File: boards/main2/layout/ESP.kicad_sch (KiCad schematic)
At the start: 15 parts, among them U13 ESP32-S3-MINI-1-N8

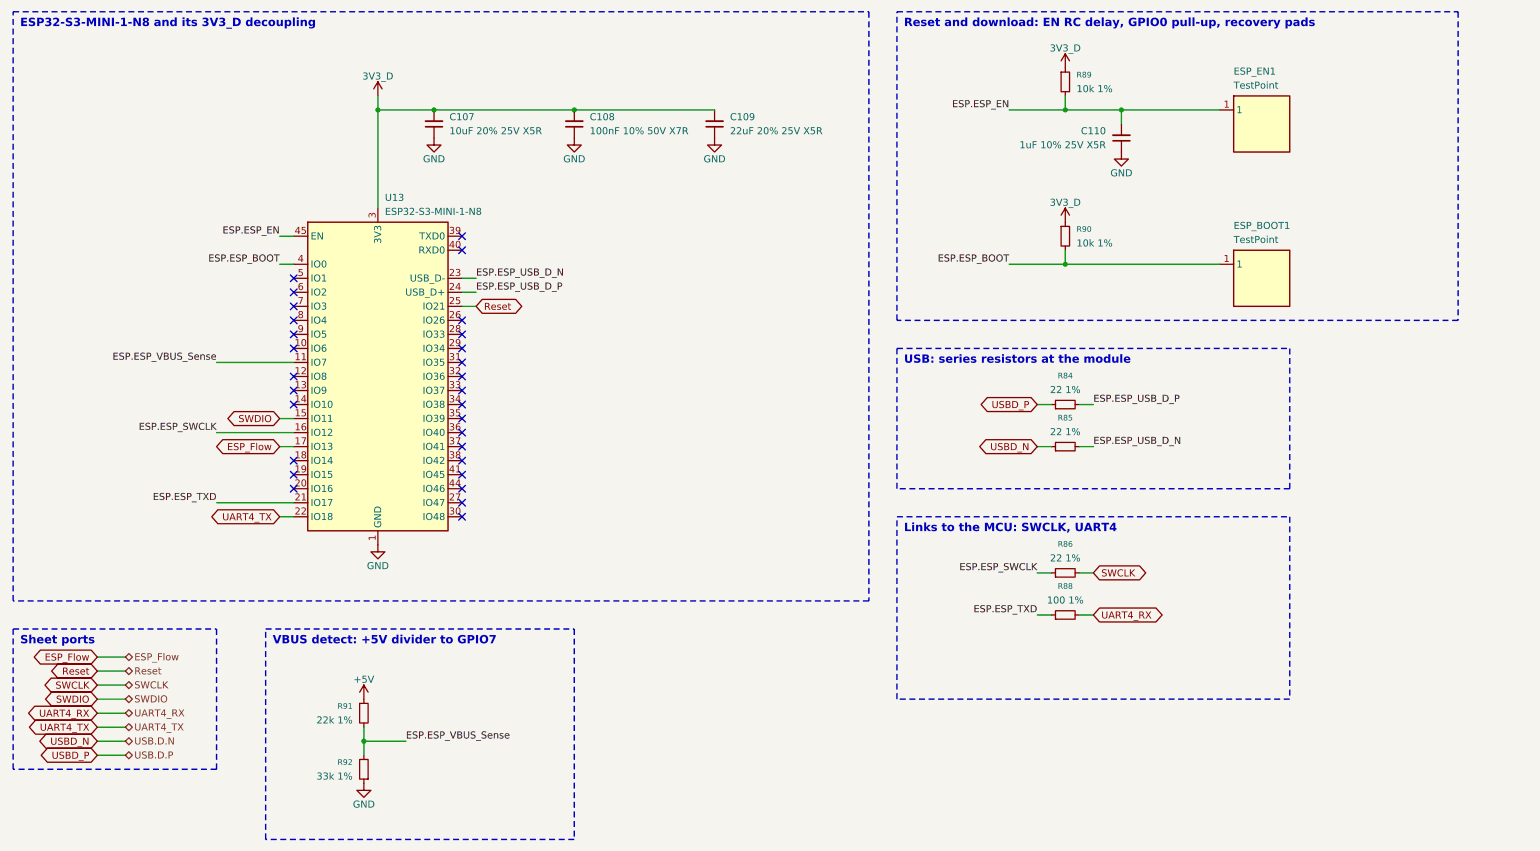
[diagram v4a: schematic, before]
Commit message: 🚧 Swap main2's USB and ESP32-S3 for an ESP32-C5 and programming headers
Schematic and component checkpoint; the layout follows in its own commit.

- Remove USB-C, its ESD, power path and VBUS sense; both MCUs flash over
  the air.
- U13 ESP32-C5-MINI-1-N4 (dual-band, 5 GHz channels 36-48) in the
  rear-right corner, with its antenna notch on the right edge. SW4 and its
  notch move to the rear-left.
- H7-C5 link: SPI2 half-duplex 3-wire (PA12 SCK, PA11 CSn, PB14 DATA with
  IOSWP), PA9 flow control, UART4 fallback on the same pins. Fan_Enable
  moves to PB10, IMU INT1 to PB6, INT2 is left open.
- J2: 2x3 1.27 mm header in the ESP-Prog layout. SWD1: 1x4 1.27 mm in
  clone ST-Link order (SWDIO, GND, SWCLK, 5V). 5V_IN feeds VSYS through
  D17 (B5819W) to flash without the battery.
- R44/R45 to 20k/2k keeps PC5 below its absolute maximum at the clamp.
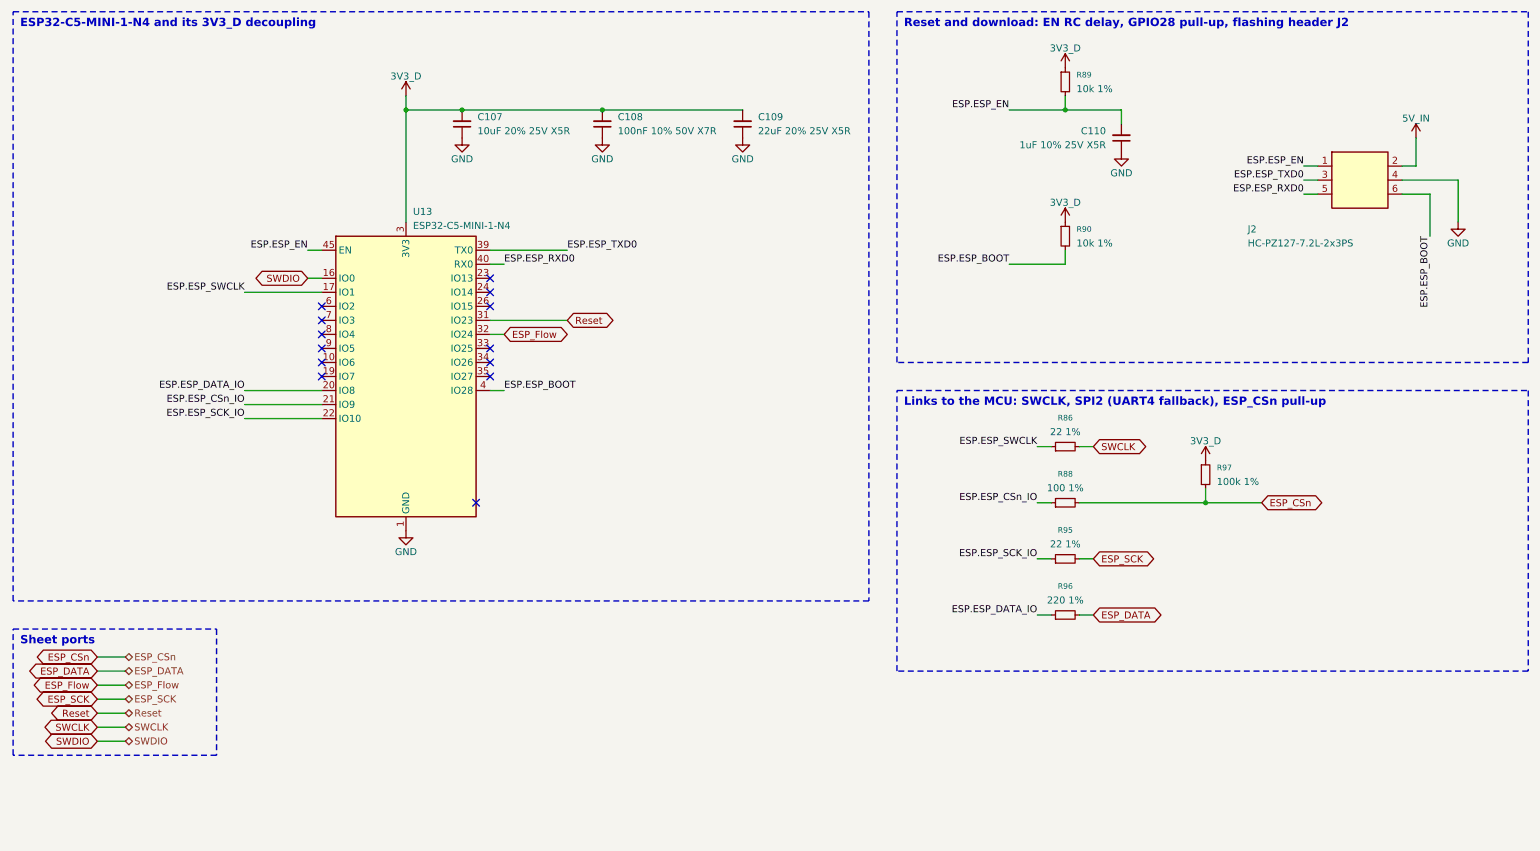
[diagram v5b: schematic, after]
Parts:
- removed ESP_BOOT1, ESP_EN1: TestPoint, Team-Micras_MicrasPCB_components_micras_TestPoint:TestPoint_Pad_D0.8mm, symbol TestPoint
- removed R84, R85: 22 1%, stdlib_kicad-footprints_Resistor_SMD:R_0402_1005Metric, symbol R_Small
- removed R91: 22k 1%, stdlib_kicad-footprints_Resistor_SMD:R_0402_1005Metric, symbol R_Small
- removed R92: 33k 1%, stdlib_kicad-footprints_Resistor_SMD:R_0402_1005Metric, symbol R_Small
- removed U13: ESP32-S3-MINI-1-N8, Team-Micras_MicrasPCB_components_espressif_ESP32-S3-MINI-1:ESP32-S3-MINI-1, symbol ESP32-S3-MINI-1
- added J2: HC-PZ127-7.2L-2x3PS, Team-Micras_MicrasPCB_components_hong-cheng_HC-PZ127-7.2L-2x3PS:HC-PZ127-7.2L-2x3PS, symbol HC-PZ127-7.2L-2x3PS
- added R95: 22 1%, stdlib_kicad-footprints_Resistor_SMD:R_0402_1005Metric, symbol R_Small
- added R96: 220 1%, stdlib_kicad-footprints_Resistor_SMD:R_0402_1005Metric, symbol R_Small
- added R97: 100k 1%, stdlib_kicad-footprints_Resistor_SMD:R_0402_1005Metric, symbol R_Small
- added U13: ESP32-C5-MINI-1-N4, Team-Micras_MicrasPCB_components_espressif_ESP32-C5-MINI-1:ESP32-C5-MINI-1, symbol ESP32-C5-MINI-1
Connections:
- net 3V3_D: now also R97.1, U13.3 (3V3)
- net ESP.ESP_BOOT: now also J2.6 (Pin_6), U13.4 (IO28)
- net ESP.ESP_EN: now also J2.1 (Pin_1), U13.45 (EN)
- net ESP.ESP_SWCLK: now also U13.17 (IO1)
- net ESP_Flow: now also U13.32 (IO24)
- net GND: now also J2.4 (Pin_4), U13.1 (GND), U13.2 (GND), U13.42 (GND), U13.43 (GND), U13.46 (GND), U13.47 (GND), U13.48 (GND), U13.50 (GND), U13.51 (GND), U13.52 (GND), U13.53 (GND), U13.54 (GND), U13.55 (GND), U13.56 (GND), U13.57 (GND), U13.58 (GND), U13.59 (GND), U13.60 (GND), U13.61 (GND), U13.62 (GND), U13.63 (GND), U13.64 (GND), U13.65 (GND)
- net Reset: now also U13.31 (IO23)
- net SWDIO: now also U13.16 (IO0)
- net ESP.ESP_TXD renamed ESP.ESP_CSn_IO
- net ESP.ESP_CSn_IO: now also U13.21 (IO9)
- net UART4_RX renamed ESP_CSn
- net ESP_CSn: now also R97.2
- new net: U13.11 (NC), U13.12 (NC), U13.13 (NC), U13.14 (NC), U13.15 (NC), U13.18 (NC), U13.25 (NC), U13.27 (NC), U13.28 (NC), U13.29 (NC), U13.30 (NC), U13.36 (NC), U13.37 (NC), U13.38 (NC), U13.41 (NC), U13.44 (NC), U13.49 (NC), U13.5 (NC)
- new net 5V_IN: J2.2 (Pin_2)
- new net ESP.ESP_DATA_IO: R96.1, U13.20 (IO8)
- new net ESP.ESP_RXD0: J2.5 (Pin_5), U13.40 (RX0)
- new net ESP.ESP_SCK_IO: R95.1, U13.22 (IO10)
- new net ESP.ESP_TXD0: J2.3 (Pin_3), U13.39 (TX0)
- new net ESP_DATA: R96.2
- new net ESP_SCK: R95.2
- no-connect marks 29 -> 13
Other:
- note added: "ESP32-C5-MINI-1-N4 and its 3V3_D decoupling"
- note added: "Links to the MCU: SWCLK, SPI2 (UART4 fallback), ESP_CSn pull-up"
- note added: "Reset and download: EN RC delay, GPIO28 pull-up, flashing header J2"
- note removed: "ESP32-S3-MINI-1-N8 and its 3V3_D decoupling"
- note removed: "Links to the MCU: SWCLK, UART4"
- note removed: "Reset and download: EN RC delay, GPIO0 pull-up, recovery pads"
- note removed: "USB: series resistors at the module"
- note removed: "VBUS detect: +5V divider to GPIO7"
- title: ESP32-S3 radio and debug probe -> ESP32-C5 radio and debug probe
- moved on the sheet: C107, C108, C109, R86, R88
